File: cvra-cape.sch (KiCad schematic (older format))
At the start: 27 parts

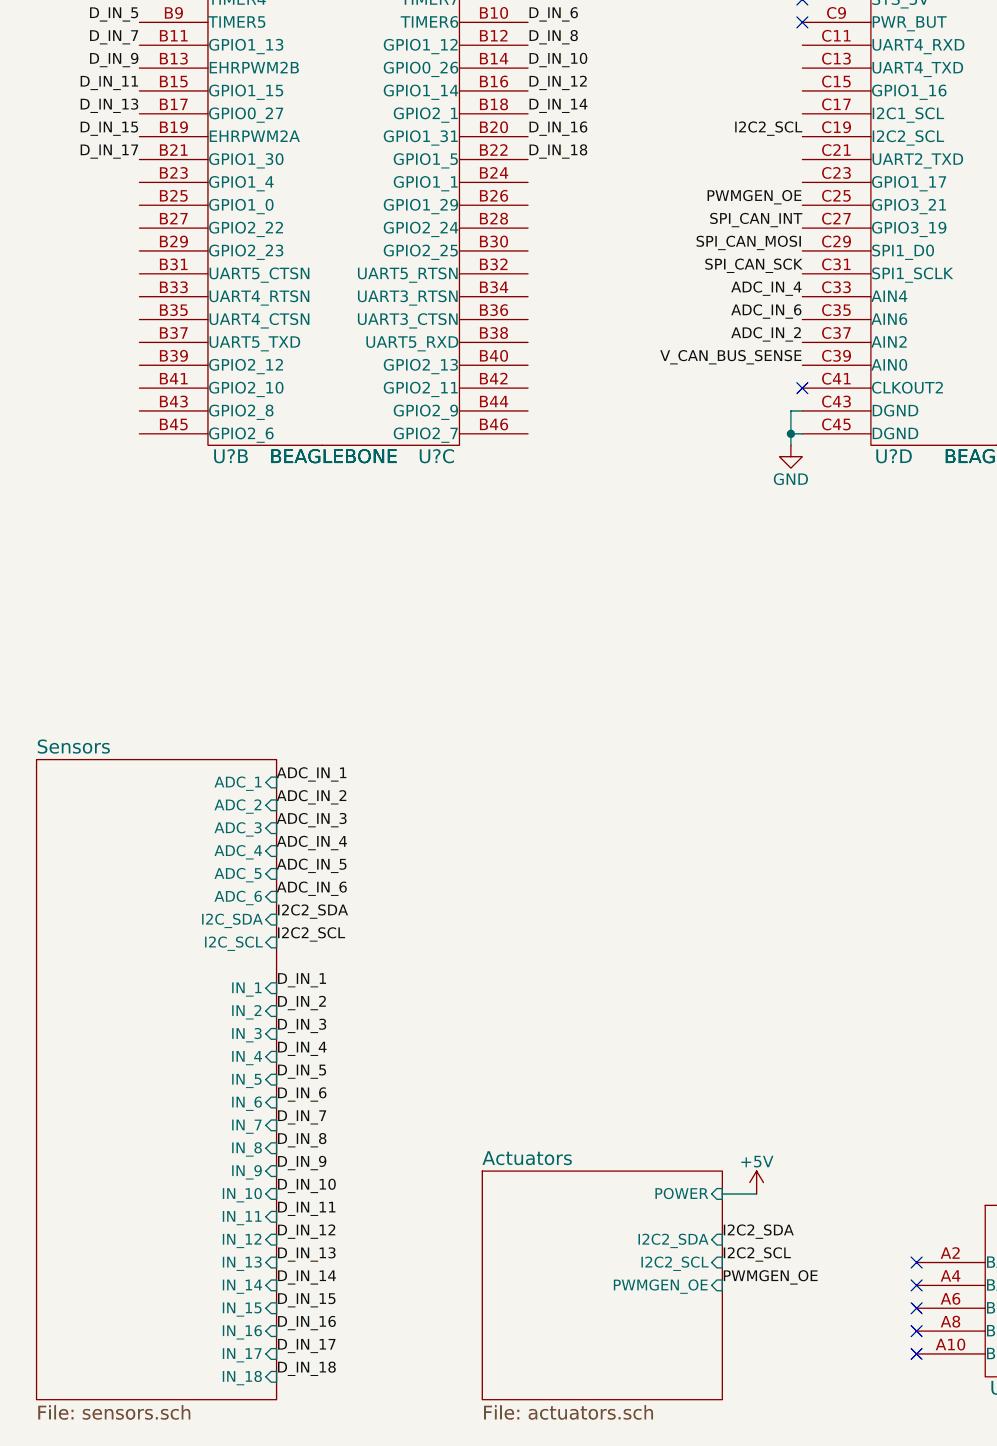
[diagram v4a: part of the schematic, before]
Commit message: Add digital outputs with NPN stage
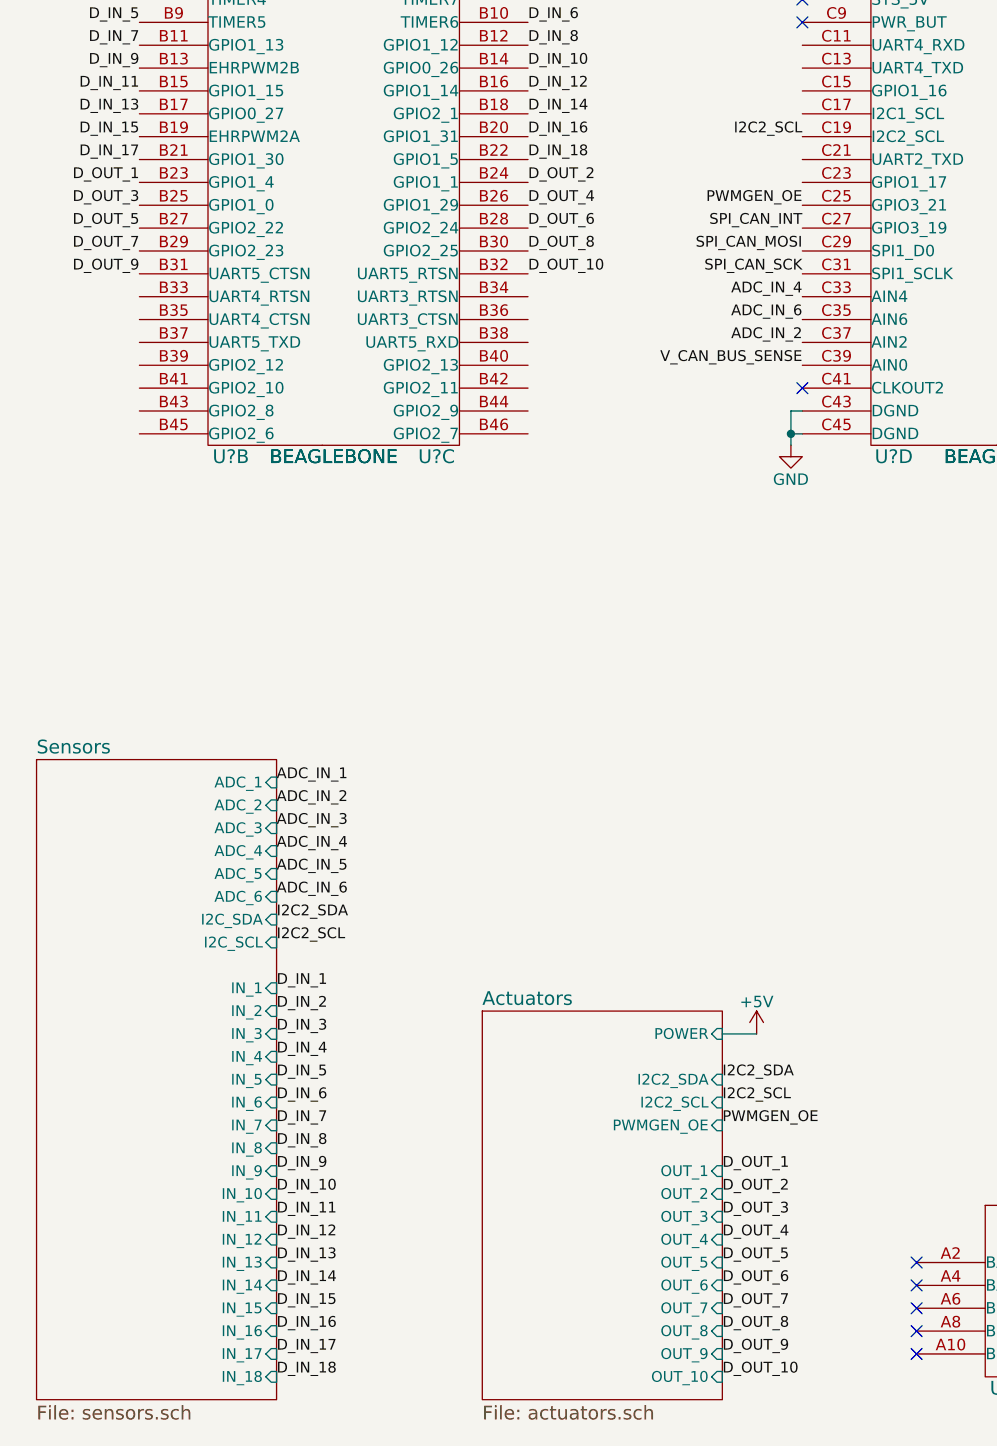
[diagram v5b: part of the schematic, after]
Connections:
- net D_OUT_1: now reaches U?.B23 (GPIO1_4)
- net D_OUT_3: now reaches U?.B25 (GPIO1_0)
- net D_OUT_5: now reaches U?.B27 (GPIO2_22)
- net D_OUT_7: now reaches U?.B29 (GPIO2_23)
- net D_OUT_9: now reaches U?.B31 (UART5_CTSN)
- net D_OUT_2: now reaches U?.B24 (GPIO1_1)
- net D_OUT_4: now reaches U?.B26 (GPIO1_29)
- net D_OUT_6: now reaches U?.B28 (GPIO2_24)
- net D_OUT_8: now reaches U?.B30 (GPIO2_25)
- net D_OUT_10: now reaches U?.B32 (UART5_RTSN)
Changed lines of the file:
@@
 	1    0    0    -1
 $EndComp
-$Sheet
-S 2800 6550 1050 1000
-U 566E12B6
-F0 "Actuators" 60
-F1 "actuators.sch" 60
-F2 "I2C2_SDA" I R 3850 6850 47
-F3 "I2C2_SCL" I R 3850 6950 47
-F4 "PWMGEN_OE" I R 3850 7050 47
-F5 "POWER" I R 3850 6650 47
-$EndSheet
 $Comp
 L C_Small C?
@@
 Text Label 7350 1575 2    47   ~ 0
 I2C2_SCL
-Text Label 3850 7050 0    47   ~ 0
+Text Label 3850 6350 0    47   ~ 0
 PWMGEN_OE
-Text Label 3850 6950 0    47   ~ 0
+Text Label 3850 6250 0    47   ~ 0
 I2C2_SCL
-Text Label 3850 6850 0    47   ~ 0
+Text Label 3850 6150 0    47   ~ 0
 I2C2_SDA
 $Sheet
@@
 L +5V #PWR?
 U 1 1 56B4D7F8
-P 4000 6650
-F 0 "#PWR?" H 4000 6500 50  0001 C CNN
-F 1 "+5V" H 4000 6790 50  0000 C CNN
-F 2 "" H 4000 6650 60  0000 C CNN
-F 3 "" H 4000 6650 60  0000 C CNN
-	1    4000 6650
-	1    0    0    -1
-$EndComp
-Wire Wire Line
-	4000 6650 3850 6650
+P 4000 5950
+F 0 "#PWR?" H 4000 5800 50  0001 C CNN
+F 1 "+5V" H 4000 6090 50  0000 C CNN
+F 2 "" H 4000 5950 60  0000 C CNN
+F 3 "" H 4000 5950 60  0000 C CNN
+	1    4000 5950
+	1    0    0    -1
+$EndComp
+Wire Wire Line
+	4000 5950 3850 5950
 Text Label 1900 5450 0    47   ~ 0
 I2C2_SDA
@@
 Text Label 3000 2125 0    47   ~ 0
 D_IN_18
+$Sheet
+S 2800 5850 1050 1700
+U 566E12B6
+F0 "Actuators" 60
+F1 "actuators.sch" 60
+F2 "I2C2_SDA" I R 3850 6150 47
+F3 "I2C2_SCL" I R 3850 6250 47
+F4 "PWMGEN_OE" I R 3850 6350 47
+F5 "POWER" I R 3850 5950 47
+F6 "OUT_1" I R 3850 6550 47
+F7 "OUT_2" I R 3850 6650 47
+F8 "OUT_3" I R 3850 6750 47
+F9 "OUT_4" I R 3850 6850 47
+F10 "OUT_5" I R 3850 6950 47
+F11 "OUT_6" I R 3850 7050 47
+F12 "OUT_7" I R 3850 7150 47
+F13 "OUT_8" I R 3850 7250 47
+F14 "OUT_9" I R 3850 7350 47
+F15 "OUT_10" I R 3850 7450 47
+$EndSheet
+Text Label 3850 6550 0    47   ~ 0
+D_OUT_1
+Text Label 3850 6650 0    47   ~ 0
+D_OUT_2
+Text Label 3850 6750 0    47   ~ 0
+D_OUT_3
+Text Label 3850 6850 0    47   ~ 0
+D_OUT_4
+Text Label 3850 6950 0    47   ~ 0
+D_OUT_5
+Text Label 3850 7050 0    47   ~ 0
+D_OUT_6
+Text Label 3850 7150 0    47   ~ 0
+D_OUT_7
+Text Label 3850 7250 0    47   ~ 0
+D_OUT_8
+Text Label 3850 7350 0    47   ~ 0
+D_OUT_9
+Text Label 3850 7450 0    47   ~ 0
+D_OUT_10
+Text Label 1300 2225 2    47   ~ 0
+D_OUT_1
+Text Label 3000 2225 0    47   ~ 0
+D_OUT_2
+Text Label 1300 2325 2    47   ~ 0
+D_OUT_3
+Text Label 3000 2325 0    47   ~ 0
+D_OUT_4
+Text Label 1300 2425 2    47   ~ 0
+D_OUT_5
+Text Label 3000 2425 0    47   ~ 0
+D_OUT_6
+Text Label 1300 2525 2    47   ~ 0
+D_OUT_7
+Text Label 3000 2525 0    47   ~ 0
+D_OUT_8
+Text Label 1300 2625 2    47   ~ 0
+D_OUT_9
+Text Label 3000 2625 0    47   ~ 0
+D_OUT_10
 $EndSCHEMATC

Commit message: Annotate
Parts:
- added CONN48: I2C, MODULE, symbol I2C
- added CONN49: UART, MODULE, symbol UART
- added R54, R55: 330, symbol R_Small
- gave numbers to parts that had none: 23
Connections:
- net +3V3: now also CONN48.1 (VCC), CONN49.1 (VCC)
- net GND: now also CONN48.2 (GND), CONN48.MECH (GND), CONN49.2 (GND), CONN49.MECH (GND)
- net I2C2_SCL: now also CONN48.3 (SCL)
- net I2C2_SDA: now also CONN48.4 (SDA)
- net UART4_RX: now reaches U3.C11 (UART4_RXD)
- net UART4_RX: now also R55.2
- net UART4_TX: now reaches U3.C13 (UART4_TXD)
- net UART4_TX: now also R54.2
- new net: CONN49.3 (TX), R54.1
- new net: CONN49.4 (RX), R55.1
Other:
- moved on the sheet: R52, R53, U3A, U3B, U3C, U3D, U3E

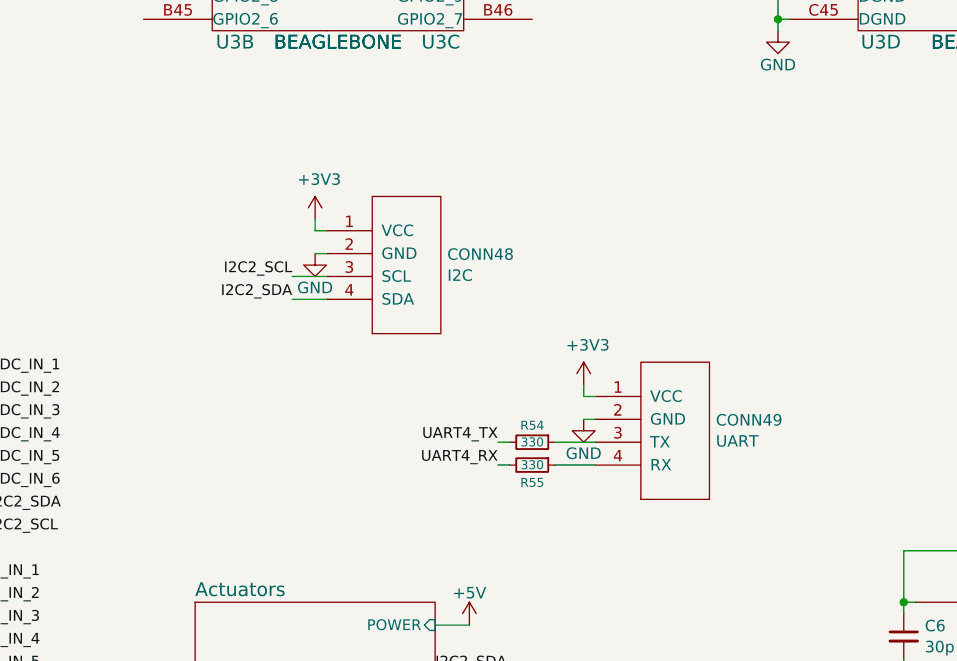
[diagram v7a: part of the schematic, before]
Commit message: Wire inputs from switches correctly
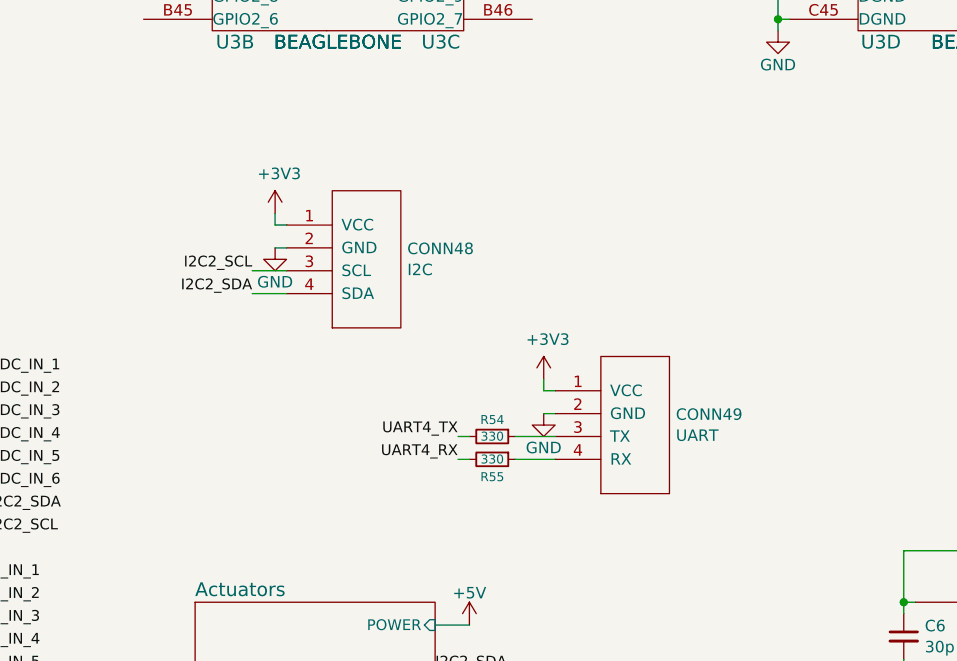
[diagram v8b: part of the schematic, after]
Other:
- moved on the sheet: CONN48, CONN49, R54, R55
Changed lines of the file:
@@
 L I2C CONN48
 U 1 1 56B9260C
-P 3725 4375
-F 0 "CONN48" H 3903 4421 50  0000 L CNN
-F 1 "I2C" H 3903 4329 50  0000 L CNN
-F 2 "MODULE" H 3725 4375 50  0001 C CNN
-F 3 "DOCUMENTATION" H 3725 4375 50  0001 C CNN
-	1    3725 4375
-	1    0    0    -1
-$EndComp
-Text Label 3225 4525 2    47   ~ 0
+P 3550 4350
+F 0 "CONN48" H 3728 4396 50  0000 L CNN
+F 1 "I2C" H 3728 4304 50  0000 L CNN
+F 2 "MODULE" H 3550 4350 50  0001 C CNN
+F 3 "DOCUMENTATION" H 3550 4350 50  0001 C CNN
+	1    3550 4350
+	1    0    0    -1
+$EndComp
+Text Label 3050 4500 2    47   ~ 0
 I2C2_SDA
-Text Label 3225 4425 2    47   ~ 0
+Text Label 3050 4400 2    47   ~ 0
 I2C2_SCL
 $Comp
 L GND #PWR5
 U 1 1 56B935CA
-P 3325 4325
-F 0 "#PWR5" H 3325 4075 50  0001 C CNN
-F 1 "GND" H 3325 4175 50  0000 C CNN
-F 2 "" H 3325 4325 50  0000 C CNN
-F 3 "" H 3325 4325 50  0000 C CNN
-	1    3325 4325
+P 3150 4300
+F 0 "#PWR5" H 3150 4050 50  0001 C CNN
+F 1 "GND" H 3150 4150 50  0000 C CNN
+F 2 "" H 3150 4300 50  0000 C CNN
+F 3 "" H 3150 4300 50  0000 C CNN
+	1    3150 4300
 	1    0    0    -1
 $EndComp
@@
 L +3V3 #PWR4
 U 1 1 56B9380F
-P 3325 4175
-F 0 "#PWR4" H 3325 4025 50  0001 C CNN
-F 1 "+3V3" H 3343 4349 50  0000 C CNN
-F 2 "" H 3325 4175 50  0000 C CNN
-F 3 "" H 3325 4175 50  0000 C CNN
-	1    3325 4175
+P 3150 4150
+F 0 "#PWR4" H 3150 4000 50  0001 C CNN
+F 1 "+3V3" H 3168 4324 50  0000 C CNN
+F 2 "" H 3150 4150 50  0000 C CNN
+F 3 "" H 3150 4150 50  0000 C CNN
+	1    3150 4150
 	1    0    0    -1
 $EndComp
@@
 	4000 5950 3850 5950
 Wire Wire Line
-	3325 4325 3375 4325
-Wire Wire Line
-	3325 4175 3325 4225
-Wire Wire Line
-	3325 4225 3375 4225
-Wire Wire Line
-	3225 4425 3375 4425
-Wire Wire Line
-	3225 4525 3375 4525
+	3150 4300 3200 4300
+Wire Wire Line
+	3150 4150 3150 4200
+Wire Wire Line
+	3150 4200 3200 4200
+Wire Wire Line
+	3050 4400 3200 4400
+Wire Wire Line
+	3050 4500 3200 4500
 Text Label 5400 1600 2    47   ~ 0
 UART4_RX
 Text Label 5400 1700 2    47   ~ 0
 UART4_TX
-Text Label 4125 5250 2    47   ~ 0
+Text Label 3950 5225 2    47   ~ 0
 UART4_RX
-Text Label 4125 5150 2    47   ~ 0
+Text Label 3950 5125 2    47   ~ 0
 UART4_TX
 $Comp
 L UART CONN49
 U 1 1 56B95F86
-P 4900 5100
-F 0 "CONN49" H 5078 5146 50  0000 L CNN
-F 1 "UART" H 5078 5054 50  0000 L CNN
-F 2 "MODULE" H 4900 5100 50  0001 C CNN
-F 3 "DOCUMENTATION" H 4900 5100 50  0001 C CNN
-	1    4900 5100
+P 4725 5075
+F 0 "CONN49" H 4903 5121 50  0000 L CNN
+F 1 "UART" H 4903 5029 50  0000 L CNN
+F 2 "MODULE" H 4725 5075 50  0001 C CNN
+F 3 "DOCUMENTATION" H 4725 5075 50  0001 C CNN
+	1    4725 5075
 	1    0    0    -1
 $EndComp
@@
 L R_Small R54
 U 1 1 56B96396
-P 4275 5150
-F 0 "R54" V 4225 5150 39  0000 C BNN
-F 1 "330" V 4275 5150 39  0000 C CNN
-F 2 "" H 4275 5150 50  0000 C CNN
-F 3 "" H 4275 5150 50  0000 C CNN
-	1    4275 5150
+P 4100 5125
+F 0 "R54" V 4050 5125 39  0000 C BNN
+F 1 "330" V 4100 5125 39  0000 C CNN
+F 2 "" H 4100 5125 50  0000 C CNN
+F 3 "" H 4100 5125 50  0000 C CNN
+	1    4100 5125
 	0    1    1    0
 $EndComp
 Wire Wire Line
-	4125 5150 4175 5150
+	3950 5125 4000 5125
 $Comp
 L R_Small R55
 U 1 1 56B97703
-P 4275 5250
-F 0 "R55" V 4375 5250 39  0000 C BNN
-F 1 "330" V 4275 5250 39  0000 C CNN
-F 2 "" H 4275 5250 50  0000 C CNN
-F 3 "" H 4275 5250 50  0000 C CNN
-	1    4275 5250
+P 4100 5225
+F 0 "R55" V 4200 5225 39  0000 C BNN
+F 1 "330" V 4100 5225 39  0000 C CNN
+F 2 "" H 4100 5225 50  0000 C CNN
+F 3 "" H 4100 5225 50  0000 C CNN
+	1    4100 5225
 	0    1    1    0
 $EndComp
 Wire Wire Line
-	4125 5250 4175 5250
+	3950 5225 4000 5225
 $Comp
 L GND #PWR9
 U 1 1 56B98317
-P 4500 5050
-F 0 "#PWR9" H 4500 4800 50  0001 C CNN
-F 1 "GND" H 4500 4900 50  0000 C CNN
-F 2 "" H 4500 5050 50  0000 C CNN
-F 3 "" H 4500 5050 50  0000 C CNN
-	1    4500 5050
-	1    0    0    -1
-$EndComp
-Wire Wire Line
-	4500 5050 4550 5050
+P 4325 5025
+F 0 "#PWR9" H 4325 4775 50  0001 C CNN
+F 1 "GND" H 4325 4875 50  0000 C CNN
+F 2 "" H 4325 5025 50  0000 C CNN
+F 3 "" H 4325 5025 50  0000 C CNN
+	1    4325 5025
+	1    0    0    -1
+$EndComp
+Wire Wire Line
+	4325 5025 4375 5025
 $Comp
 L +3V3 #PWR8
 U 1 1 56B9886E
-P 4500 4900
-F 0 "#PWR8" H 4500 4750 50  0001 C CNN
-F 1 "+3V3" H 4518 5074 50  0000 C CNN
-F 2 "" H 4500 4900 50  0000 C CNN
-F 3 "" H 4500 4900 50  0000 C CNN
-	1    4500 4900
-	1    0    0    -1
-$EndComp
-Wire Wire Line
-	4500 4900 4500 4950
-Wire Wire Line
-	4500 4950 4550 4950
-Wire Wire Line
-	4375 5150 4550 5150
-Wire Wire Line
-	4375 5250 4550 5250
+P 4325 4875
+F 0 "#PWR8" H 4325 4725 50  0001 C CNN
+F 1 "+3V3" H 4343 5049 50  0000 C CNN
+F 2 "" H 4325 4875 50  0000 C CNN
+F 3 "" H 4325 4875 50  0000 C CNN
+	1    4325 4875
+	1    0    0    -1
+$EndComp
+Wire Wire Line
+	4325 4875 4325 4925
+Wire Wire Line
+	4325 4925 4375 4925
+Wire Wire Line
+	4200 5125 4375 5125
+Wire Wire Line
+	4200 5225 4375 5225
 $EndSCHEMATC
